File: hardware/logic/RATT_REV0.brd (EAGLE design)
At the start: 194.3 x 76.2 mm, 129 parts, among them IC1 TLP292-4, IC13 MCP73831, IC16 PCA9539PW, IC2 CPC1002N, IC3 CPC1002N, IC4 CPC1002N, IC5 CPC1002N, J1 4P-2.0, J2 4P-2.0, J3 F-1X06-SIP-100-40, J4 4P-2.0, J6 4P-2.0, J7 PHOENIX1803484, J8 PHOENIX1803484, Q1 2.5A/30V, Q2 MBT3904DW1T1, Q3 2.5A/30V, Q5 2N7002, Q6 2.5A/30V, U1 RPI-ZERO, U5 AP2112K-3.3V

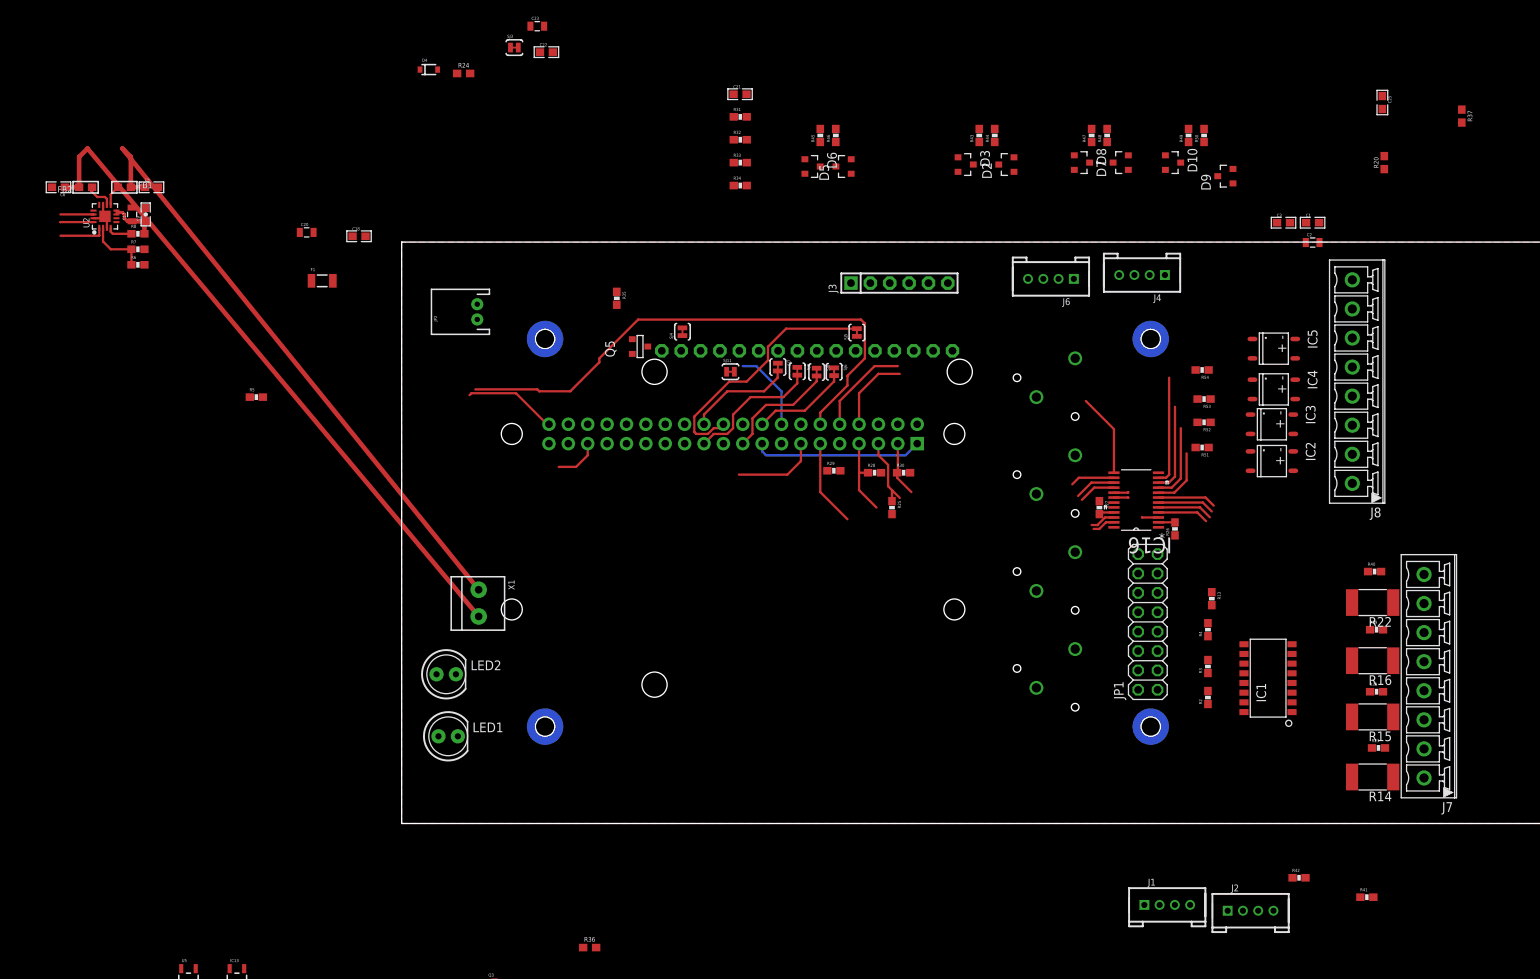
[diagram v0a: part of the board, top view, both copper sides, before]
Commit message: Lots o' routing
Screen, Pi, audio, preliminary IO routed
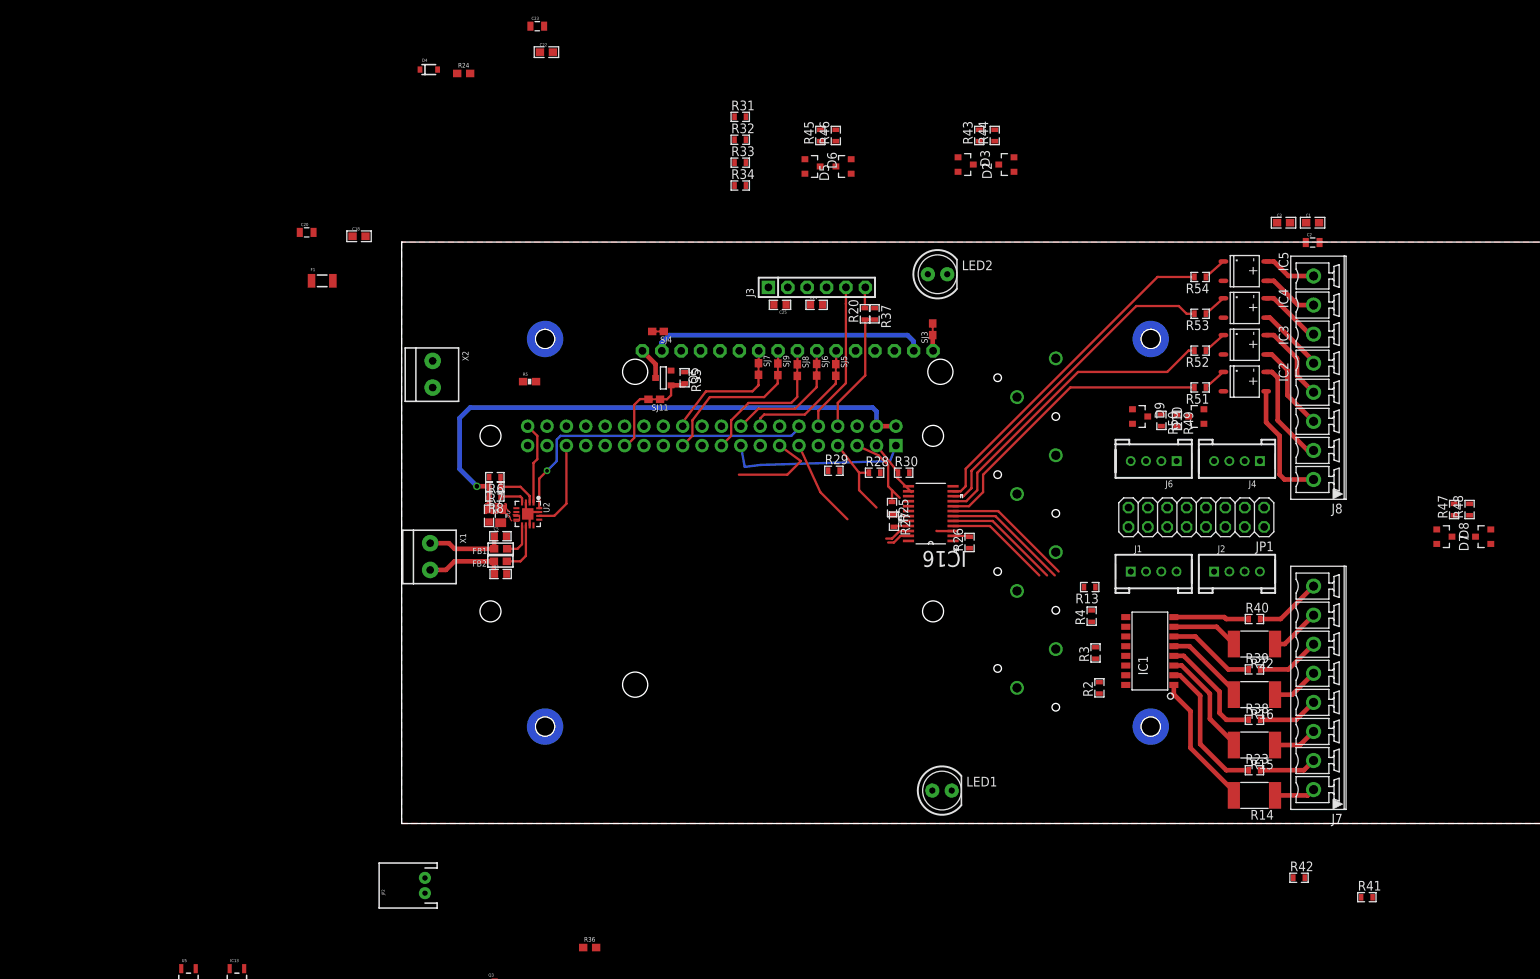
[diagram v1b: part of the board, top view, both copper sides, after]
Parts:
- added X2: (no value), Adafruit_MAX98357:TERMBLOCK_1X2-3.5MM
- C17: device SparkFun-Capacitors:0805@1 -> MakeItLabs:0805-CAP
- C21, C25, C5, C6: device SparkFun-Capacitors:0603-CAP@1 -> MakeItLabs:0603-CAP
- C9: device SparkFun-Passives:0603-CAP -> MakeItLabs:0603-CAP
- R13, R2, R25, R26, R27, R28, R29, R3, R30, R31, R32, R33, R34, R4, R41, R42, R43, R44, R45, R46, R47, R48, R49, R50, R6, R7: device SparkFun-Resistors:0603-RES -> MakeItLabs:0603-RES
- R20, R37: device SparkFun-Resistors:0603 -> MakeItLabs:0603-RES
- R23, R35, R38, R39, R40, R51, R52, R53, R54: device SparkFun-Passives:0603-RES -> MakeItLabs:0603-RES
- R8: value 500K -> 680K; device SparkFun-Resistors:0603-RES -> MakeItLabs:0603-RES
- SJ11, SJ3, SJ4, SJ5, SJ6, SJ7, SJ8, SJ9: device SparkFun-Passives:PAD-JUMPER-2-NC_BY_TRACE_YES_SILK -> MakeItLabs:SOLDERJUMPER_10MIL
- moved C25 83.3 mm to (49.6, 68.0), turned to 180 degrees
- moved LED2 83.0 mm to (70.2, 72.0)
- moved R37 81.2 mm to (62.0, 66.8)
- moved C6 77.0 mm to (13.0, 32.7), turned to 0 degrees
- moved JP2 75.5 mm to (3.05, -8.13)
- moved FB2 73.2 mm to (12.9, 34.4)
- moved R20 70.9 mm to (60.7, 66.8)
- moved FB1 68.4 mm to (13.0, 36.0), turned to 180 degrees
- moved D7 68.3 mm to (141.7, 37.6)
- moved D8 68.3 mm to (136.7, 37.6)
- moved R47 68.3 mm to (137.9, 41.1)
- moved R48 68.3 mm to (140.0, 41.1)
- moved U2 67.8 mm to (16.5, 40.6), turned to 270 degrees
- moved SJ3 66.1 mm to (69.6, 64.8), turned to 90 degrees
- moved LED1 65.1 mm to (70.8, 4.32)
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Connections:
- removed net !LED0: U1.29
- removed net N$13: U1.26
- net +3V3: no longer R8.2
- net +5V: now also X2.1
- net 5V_RFID_TX: now also J3.6; no longer J3.5
- net GND: now also X2.2
- net LCD_BACKLIGHT: now also U1.29; no longer U1.16
- net LCD_RESET: now also U1.16; no longer U1.22
- net RFID_RX: now also J3.5; no longer J3.6
- net VIN: now also R8.2
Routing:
- net N$6: track 87.3 -> 10.5 mm
- net N$7: track 81.7 -> 10.3 mm
- net VIN: track 5.23 -> 74.6 mm, vias 0 -> 1
- net N$26: track 0.00 -> 36.1 mm
- net I2S_BCK: track 75.5 -> 42.6 mm, vias 0 -> 1
- net OUT2: track 11.6 -> 43.7 mm
- net OUT0: track 7.90 -> 39.4 mm
- net OUT1: track 10.0 -> 41.1 mm
- net OUT3: track 14.3 -> 44.9 mm
- net LCD_RESET: track 33.6 -> 13.8 mm
- net N$15: track 0.00 -> 18.7 mm
- net N$19: track 0.00 -> 17.7 mm
- net N$32: track 0.00 -> 16.4 mm
- net N$36: track 0.00 -> 14.9 mm
- net N$39: track 0.00 -> 14.3 mm
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- added copper zone on layer 1, net VIN
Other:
- board text added: "C:/Users/Adam/Documents/GitHub/ratt/hardware/references/oshw-logo_bw.bmp"

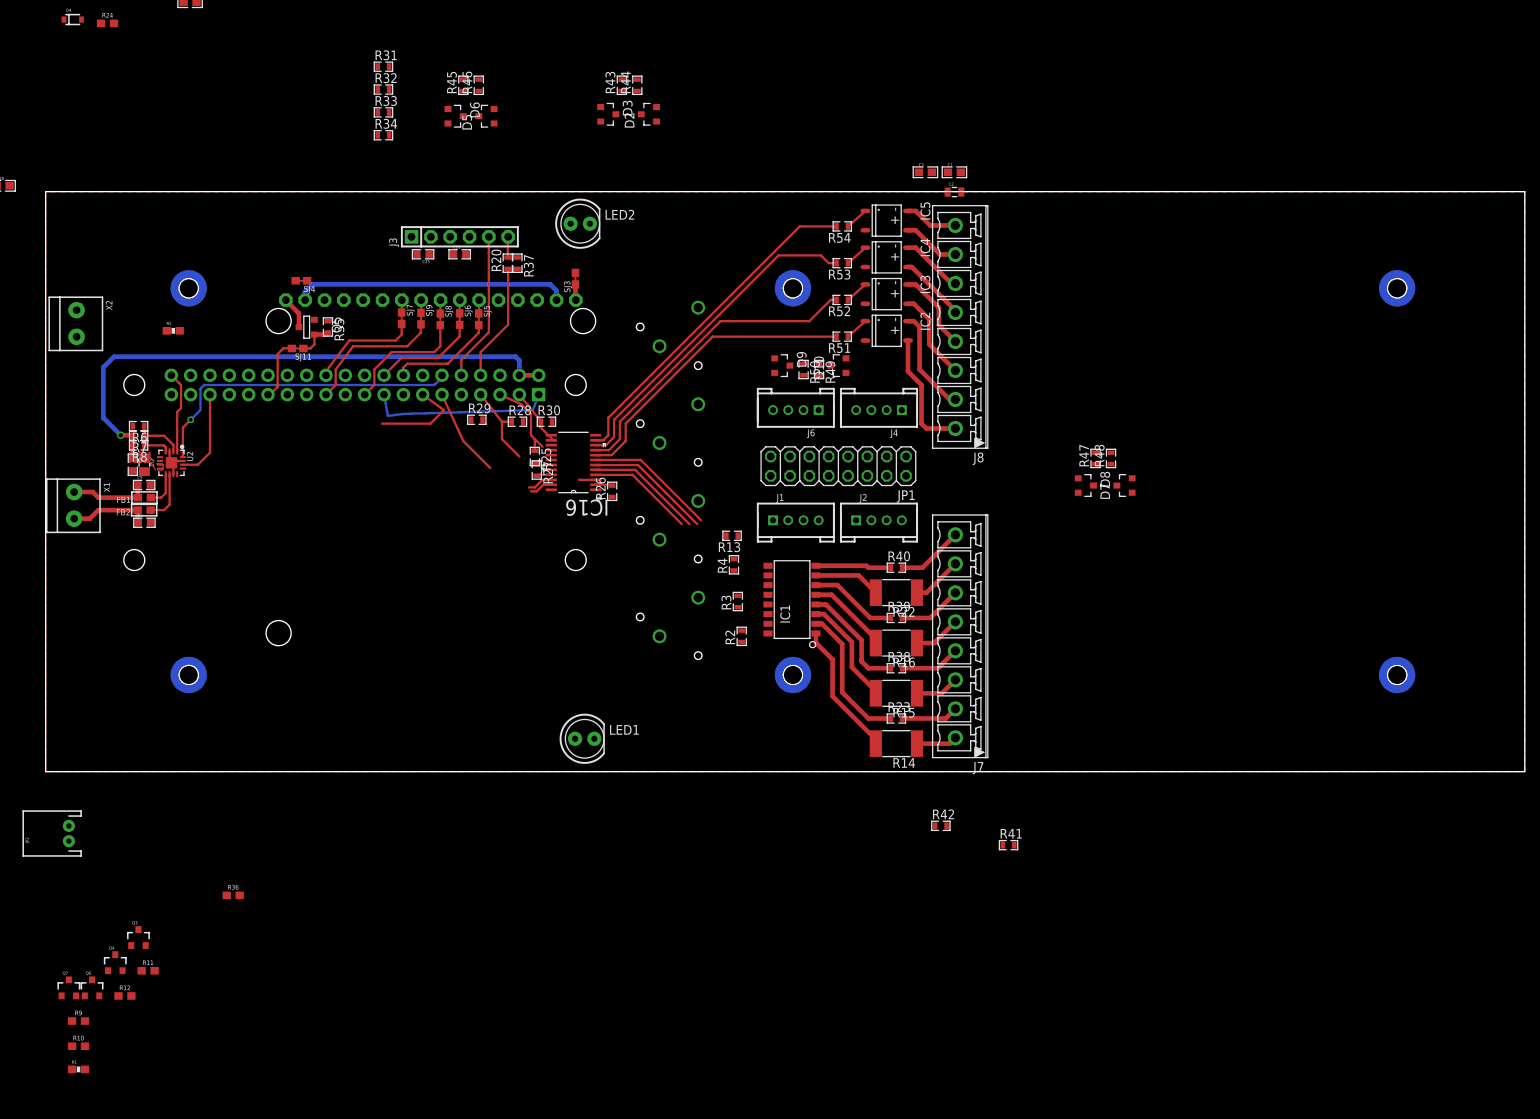
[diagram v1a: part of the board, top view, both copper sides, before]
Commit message: Lot's O' routin'
Board resized to 3x5"
I/O 100% placed and routed
LEDs placed and routed
I/O chip routed
Todo: Power stuff
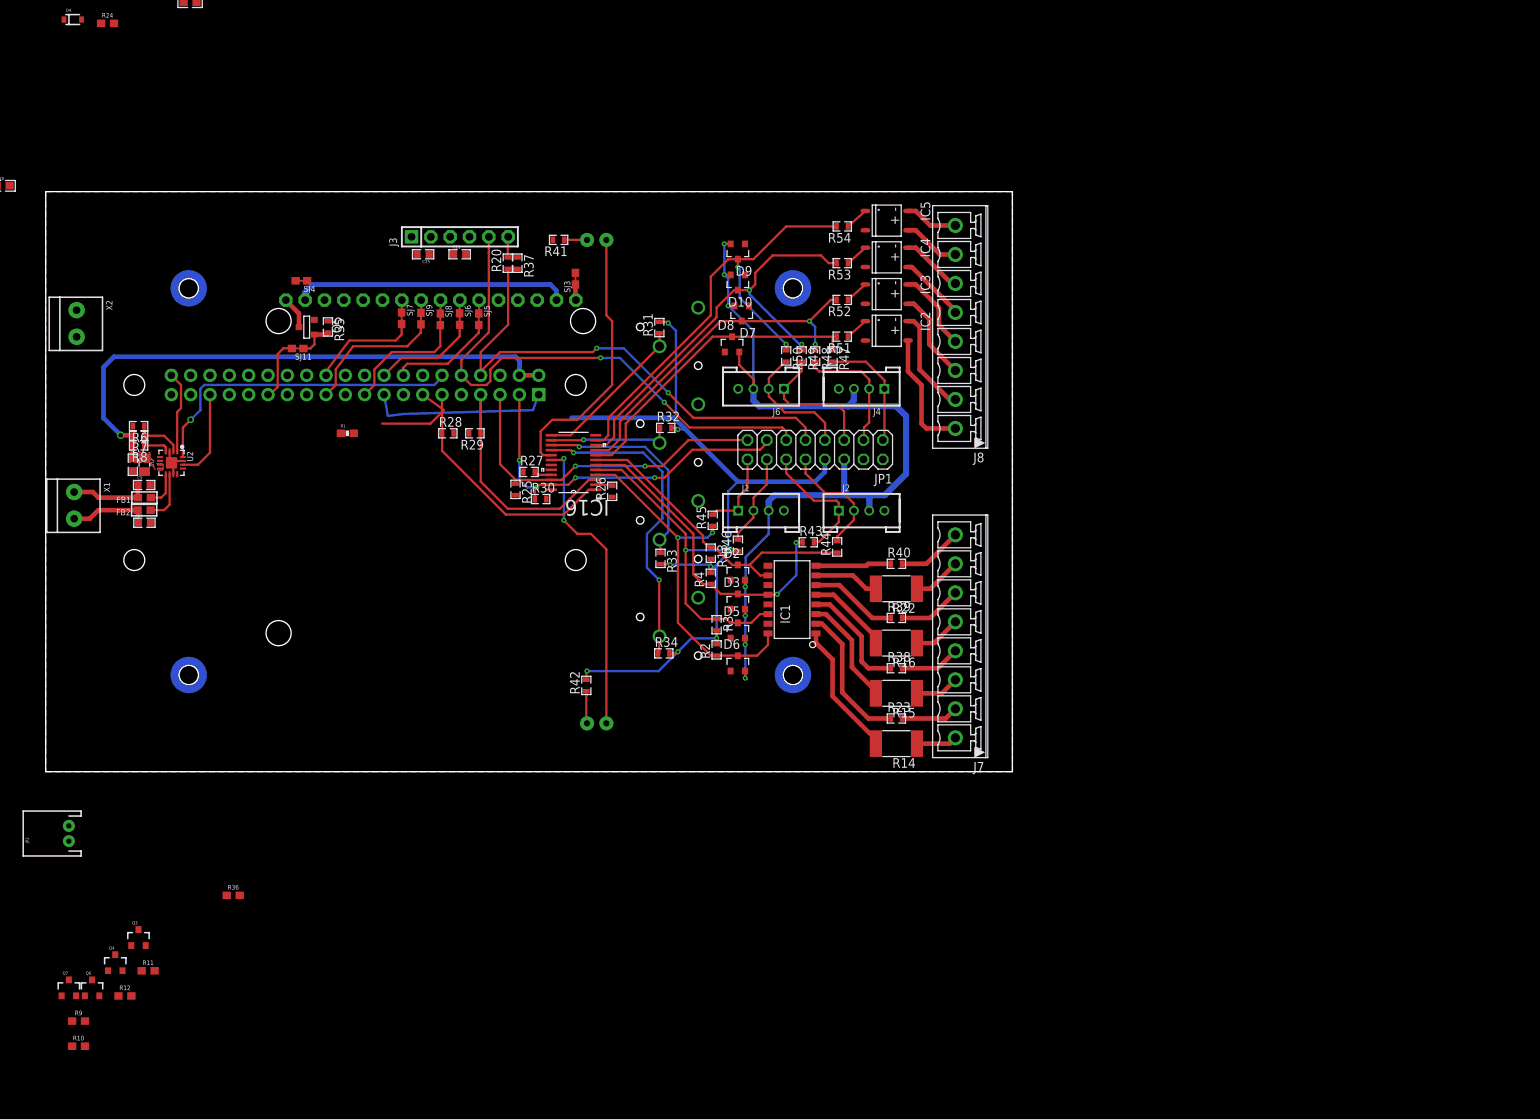
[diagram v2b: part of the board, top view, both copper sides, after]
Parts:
- removed C1, C3: 0.1uF, SparkFun-Capacitors:0603-CAP@1
- removed C2: 10uF, SparkFun-Capacitors:0805@1
- removed R5: 10K, SparkFun-Resistors:0603-RES
- moved R41 99.1 mm to (67.4, 69.9), turned to 180 degrees
- moved R1 90.7 mm to (39.6, 44.5)
- moved D6 80.9 mm to (90.9, 14.2), turned to 0 degrees
- moved R34 77.4 mm to (81.2, 15.5)
- moved D5 75.2 mm to (90.9, 18.5), turned to 0 degrees
- moved R46 69.4 mm to (90.9, 29.7)
- moved R33 69.0 mm to (80.8, 28.0), turned to 270 degrees
- moved D3 66.2 mm to (90.9, 22.4), turned to 0 degrees
- moved R44 66.1 mm to (104.0, 29.5)
- moved R45 65.9 mm to (87.6, 33.0)
- moved LED2 65.7 mm to (72.4, 6.35), flipped to the bottom, turned to 180 degrees
- moved LED1 65.6 mm to (72.4, 69.8), flipped to the bottom, turned to 180 degrees
- moved R43 64.8 mm to (100.2, 30.1), turned to 0 degrees
- moved D2 61.3 mm to (90.9, 26.2), turned to 0 degrees
- moved R32 57.9 mm to (81.5, 45.2)
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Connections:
- removed net N$8: C2.1, R5.2
- removed net ~RESET: C3.1
- net !I/O_IRQ: now also U1.11; no longer U1.7
- net !I/O_RESET: now also U1.7; no longer U1.11
- net +3V3: now also JP1.8; no longer JP1.3
- net +5V: now also JP1.6; no longer JP1.5
- net GND: now also JP1.2, JP1.4; no longer C2.2, C3.2, JP1.1, JP1.7
- net I2C_SCL: now also JP1.15; no longer JP1.9
- net I2C_SDA: now also JP1.13; no longer JP1.11
- net IN0P: now also JP1.16; no longer JP1.2
- net IN1P: now also JP1.14; no longer JP1.4
- net IN2P: now also JP1.12; no longer JP1.6
- net IN3P: now also JP1.10; no longer JP1.8
- net OUT0P: now also JP1.1; no longer JP1.10
- net OUT1P: now also JP1.3; no longer JP1.12
- net OUT2P: now also JP1.5; no longer JP1.14
- net OUT3P: now also JP1.7; no longer JP1.16
- net RFID_RX: now also JP1.11; no longer JP1.15
- net RFID_TX: now also JP1.9; no longer JP1.13
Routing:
- net +5V: track 0.00 -> 115.8 mm, vias 0 -> 7
- net +3V3: track 0.00 -> 109.1 mm, vias 0 -> 7
- net RFID_RX: track 19.7 -> 70.4 mm, vias 0 -> 2
- net RFID_TX: track 16.8 -> 67.2 mm, vias 0 -> 2
- net !BUTTON3: track 0.00 -> 41.3 mm, vias 0 -> 2
- net LED1: track 0.00 -> 39.9 mm, vias 0 -> 2
- net I2C_SDA: track 10.9 -> 48.5 mm, vias 0 -> 4
- net LED0: track 0.00 -> 35.6 mm
- net IN0: track 14.0 -> 46.8 mm, vias 0 -> 2
- net I2C_SCL: track 14.7 -> 45.2 mm, vias 0 -> 2
- net IN1: track 15.3 -> 43.7 mm, vias 0 -> 2
- net !BUTTON2: track 0.00 -> 28.2 mm, vias 0 -> 1
- net IN2: track 16.6 -> 42.7 mm, vias 0 -> 2
- net IN3: track 17.1 -> 41.5 mm
- net !I/O_IRQ: track 11.3 -> 32.4 mm
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- added copper zone on layer 16, net GND
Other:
- board size 194.3 x 76.2 mm -> 127 x 76.2 mm
